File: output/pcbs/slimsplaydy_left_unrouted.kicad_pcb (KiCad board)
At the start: 2 copper layers, 115.1 x 87.3 mm, 20 parts

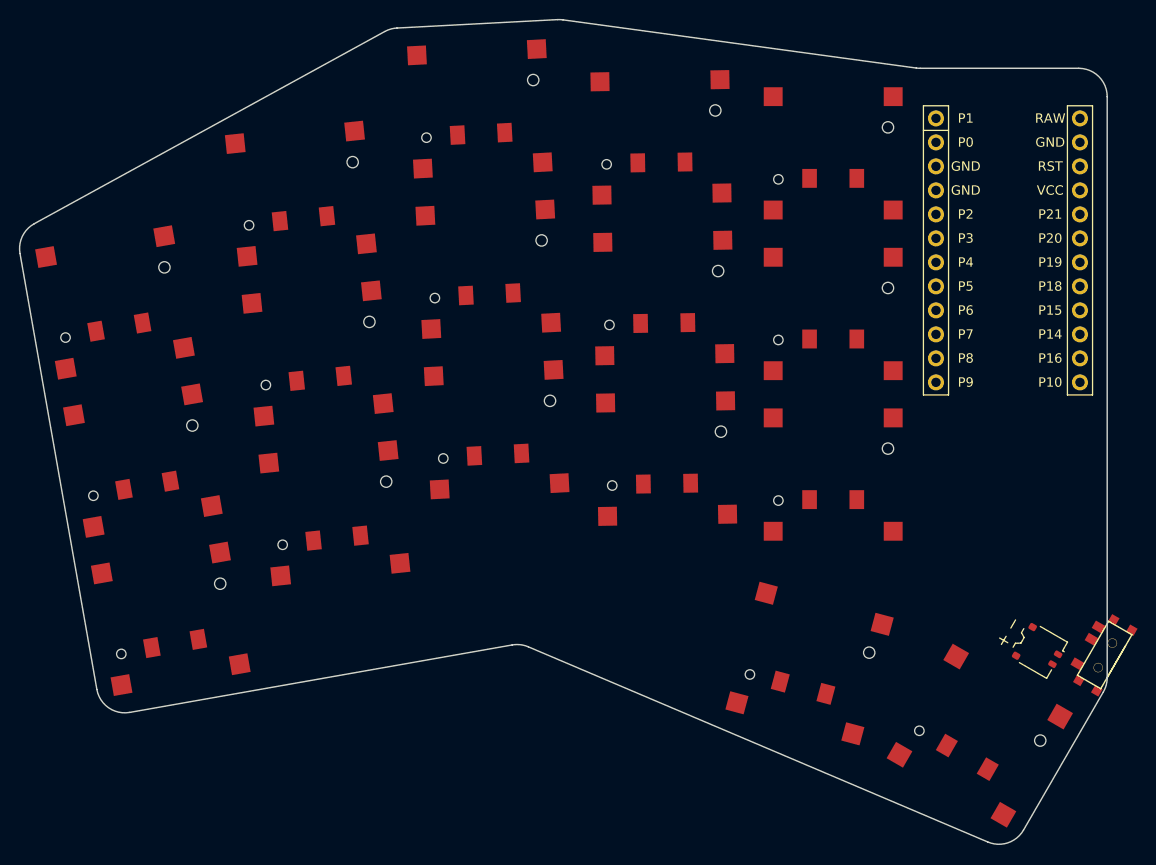
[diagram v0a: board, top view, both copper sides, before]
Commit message: Add battery footprint, change outline.
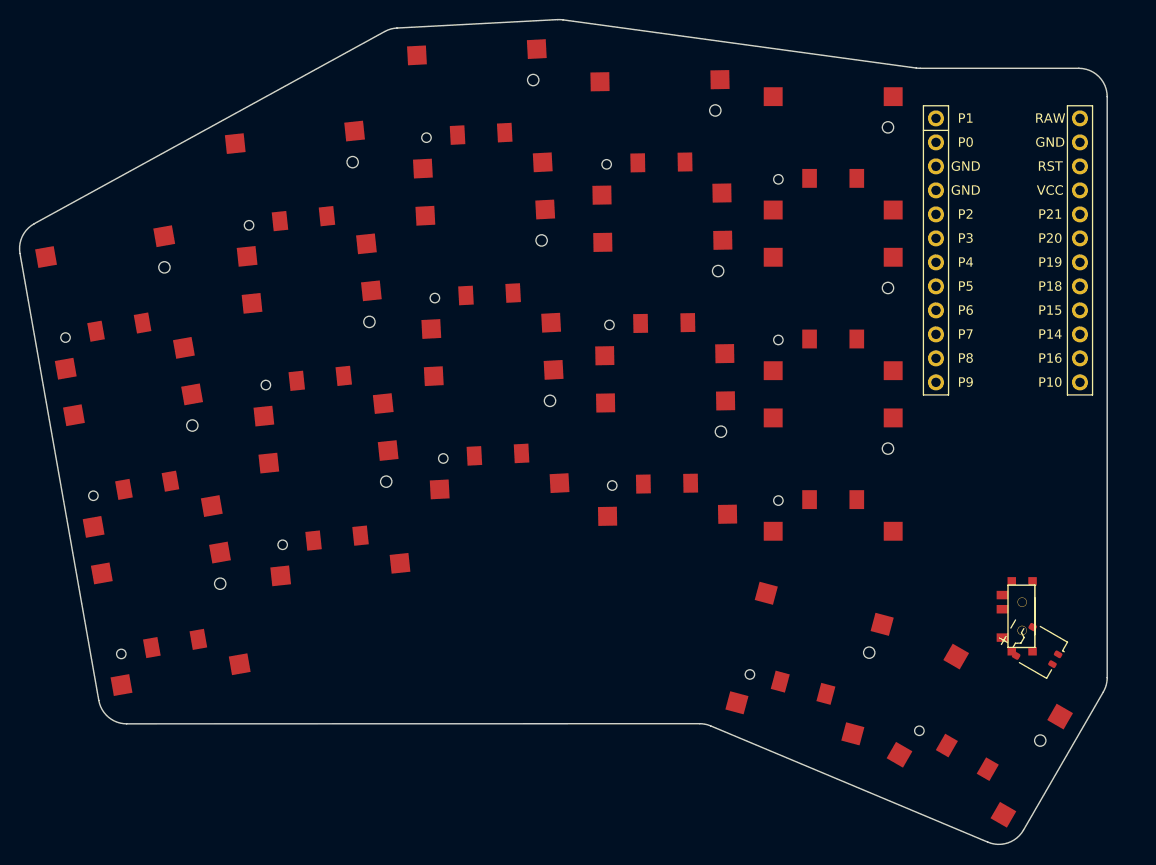
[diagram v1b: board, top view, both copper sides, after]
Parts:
- added XX1: , Battery_301230, F.Cu at (129.7, 140.4)
- moved T1 9.72 mm to (196.7, 143.4), turned to -90 degrees
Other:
- outline, holes or cut-outs redrawn
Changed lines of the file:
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@@
   )
         (module E73:SPDT_C128955 (layer F.Cu)
-            (at 205.4748588 147.5445331 -120)
+            (at 196.6773593 143.4119143 -90)
             (fp_text reference "T1" (at 0 0) (layer F.SilkS) hide (effects (font (size 1.27 1.27) (thickness 0.15))))
             (fp_text value "" (at 0 0) (layer F.SilkS) hide (effects (font (size 1.27 1.27) (thickness 0.15))))
@@
             (pad "" np_thru_hole circle (at 1.5 0) (size 1 1) (drill 0.9) (layers *.Cu *.Mask))
             (pad "" np_thru_hole circle (at -1.5 0) (size 1 1) (drill 0.9) (layers *.Cu *.Mask))
-            (pad 1 smd rect (at 2.25 2.075 -120) (size 0.9 1.25) (layers F.Cu F.Paste F.Mask) (net 67 "BAT_P"))
-            (pad 2 smd rect (at -0.75 2.075 -120) (size 0.9 1.25) (layers F.Cu F.Paste F.Mask) (net 68 "BAT"))
-            (pad 3 smd rect (at -2.25 2.075 -120) (size 0.9 1.25) (layers F.Cu F.Paste F.Mask))
-            (pad "" smd rect (at 3.7 -1.1 -120) (size 0.9 0.9) (layers F.Cu F.Paste F.Mask))
-            (pad "" smd rect (at 3.7 1.1 -120) (size 0.9 0.9) (layers F.Cu F.Paste F.Mask))
-            (pad "" smd rect (at -3.7 1.1 -120) (size 0.9 0.9) (layers F.Cu F.Paste F.Mask))
-            (pad "" smd rect (at -3.7 -1.1 -120) (size 0.9 0.9) (layers F.Cu F.Paste F.Mask))
+            (pad 1 smd rect (at 2.25 2.075 -90) (size 0.9 1.25) (layers F.Cu F.Paste F.Mask) (net 67 "BAT_P"))
+            (pad 2 smd rect (at -0.75 2.075 -90) (size 0.9 1.25) (layers F.Cu F.Paste F.Mask) (net 68 "BAT"))
+            (pad 3 smd rect (at -2.25 2.075 -90) (size 0.9 1.25) (layers F.Cu F.Paste F.Mask))
+            (pad "" smd rect (at 3.7 -1.1 -90) (size 0.9 0.9) (layers F.Cu F.Paste F.Mask))
+            (pad "" smd rect (at 3.7 1.1 -90) (size 0.9 0.9) (layers F.Cu F.Paste F.Mask))
+            (pad "" smd rect (at -3.7 1.1 -90) (size 0.9 0.9) (layers F.Cu F.Paste F.Mask))
+            (pad "" smd rect (at -3.7 -1.1 -90) (size 0.9 0.9) (layers F.Cu F.Paste F.Mask))
         )
   (footprint "ceoloide:battery_connector_molex_pico_ezmate_1x02"
@@
     (fp_line (start 0.45 2.02) (end 0.75 2.52) (layer "F.Fab") (stroke (width 0.1) (type solid)))
   )
-  (gr_line (start 205.27476762503858 151.4085073312824) (end 196.81826658790172 166.04055279537687) (angle 90) (layer Edge.Cuts) (width 0.15))
-(gr_line (start 193.047946514134 167.30060611800113) (end 144.40253976719455 146.6369199984339) (angle 90) (layer Edge.Cuts) (width 0.15))
-(gr_line (start 142.7086834385818 146.44370619182033) (end 102.22231583096315 153.58254515415393) (angle 90) (layer Edge.Cuts) (width 0.15))
-(gr_line (start 98.74694796516516 151.14906644812334) (end 90.61156255294658 105.01100333847262) (angle 90) (layer Edge.Cuts) (width 0.15))
-(gr_line (start 92.12349826198067 101.85961590074879) (end 129.22108122867328 81.51597017246681) (angle 90) (layer Edge.Cuts) (width 0.15))
+(footprint "Battery_301230"
+(at 129.6773593 140.4119143 0)
+(layer "F.Cu")
+(property "Reference" "XX1" hide (at 0 0 0) (layer "F.SilkS") (effects (font (size 1 1) (thickness 0.15))))
+(descr "Nothing but silk, 35x15 for a little extra padding")
+(tags "Battery Lithium 301230")
+(attr smd board_only exclude_from_bom)
+(embedded_fonts no)
+(zone (net 0) (net_name "") (layer "F.SilkS")  (hatch edge 0.5) (connect_pads (clearance 0)) (min_thickness 0.25) (filled_areas_thickness no) (keepout (tracks allowed) (vias allowed) (pads not_allowed) (copperpour allowed) (footprints not_allowed)) (placement (enabled no) (sheetname "")) (fill (thermal_gap 0.5) (thermal_bridge_width 0.5)) (polygon (pts (xy 129.677 140.412) (xy 163.677 140.412) (xy 163.677 154.412) (xy 129.677 154.412))))
+)
+  (gr_line (start 205.27476762503855 151.4085073312824) (end 196.812189609797 166.0510676193593) (angle 90) (layer Edge.Cuts) (width 0.15))
+(gr_line (start 193.05444906405054 167.31643081205561) (end 163.71171454116796 155.0095167067306) (angle 90) (layer Edge.Cuts) (width 0.15))
+(gr_line (start 162.55058342048673 154.77603615610332) (end 101.90742581681184 154.79218459658966) (angle 90) (layer Edge.Cuts) (width 0.15))
+(gr_line (start 98.95220363092409 152.3131292764732) (end 90.61156255219102 105.01100333888701) (angle 90) (layer Edge.Cuts) (width 0.15))
+(gr_line (start 92.12349826122507 101.85961590116315) (end 129.22108122867328 81.51597017246681) (angle 90) (layer Edge.Cuts) (width 0.15))
 (gr_line (start 130.50656080060108 81.15052443580738) (end 147.51504570837903 80.25914752326048) (angle 90) (layer Edge.Cuts) (width 0.15))
 (gr_line (start 148.07755649811176 80.28256782932584) (end 185.4755427700766 85.38438268843433) (angle 90) (layer Edge.Cuts) (width 0.15))
 (gr_line (start 185.88104555485685 85.4119144) (end 202.6773593 85.4119144) (angle 90) (layer Edge.Cuts) (width 0.15))
-(gr_line (start 205.6773593 88.4119144) (end 205.6773593 149.90735117460594) (angle 90) (layer Edge.Cuts) (width 0.15))
-(gr_arc (start 194.22085826286315 164.5393966387004) (end 193.04794646286314 167.3006061387004) (angle -82.9894051945816) (layer Edge.Cuts) (width 0.15))
-(gr_arc (start 143.22962801846543 149.39812947773467) (end 144.40253981846544 146.63691997773466) (angle -33.0149065103478) (layer Edge.Cuts) (width 0.15))
-(gr_arc (start 101.70137125107951 150.62812186823956) (end 98.7469479510795 151.14906646823957) (angle -89.99999999999747) (layer Edge.Cuts) (width 0.15))
-(gr_arc (start 93.56598583886094 104.49005875858893) (end 92.12349823886093 101.85961585858892) (angle -71.26042897748029) (layer Edge.Cuts) (width 0.15))
+(gr_line (start 205.6773593 88.4119144) (end 205.6773593 149.90735117460588) (angle 90) (layer Edge.Cuts) (width 0.15))
+(gr_arc (start 194.2147812847584 164.54991146268281) (end 193.0544490847584 167.3164307626828) (angle -82.72862751199224) (layer Edge.Cuts) (width 0.15))
+(gr_arc (start 162.55138232046008 157.77603605610335) (end 163.71171452046008 155.00951675610335) (angle -22.76938590082807) (layer Edge.Cuts) (width 0.15))
+(gr_arc (start 101.90662691683843 151.79218469658963) (end 98.95220361683843 152.31312929658964) (angle -80.01525707307042) (layer Edge.Cuts) (width 0.15))
+(gr_arc (start 93.56598583810536 104.49005875900332) (end 92.12349823810536 101.85961585900331) (angle -71.26042897748013) (layer Edge.Cuts) (width 0.15))
 (gr_arc (start 130.66356880555355 84.14641303030704) (end 130.50656080555356 81.15052443030704) (angle -25.739569207300832) (layer Edge.Cuts) (width 0.15))
 (gr_arc (start 147.6720537133315 83.25503611776017) (end 148.0775565133315 80.28256791776018) (angle -10.76831370557288) (layer Edge.Cuts) (width 0.15))
 (gr_arc (start 185.88104555485685 82.4119144) (end 185.47554275485686 85.3843826) (angle -7.768311097698927) (layer Edge.Cuts) (width 0.15))
 (gr_arc (start 202.6773593 88.4119144) (end 205.6773593 88.4119144) (angle -90) (layer Edge.Cuts) (width 0.15))
-(gr_arc (start 202.6773593 149.90735117460594) (end 205.2747677 151.40850737460593) (angle -30.02550052311193) (layer Edge.Cuts) (width 0.15))
+(gr_arc (start 202.6773593 149.90735117460588) (end 205.2747677 151.40850737460588) (angle -30.02550052311318) (layer Edge.Cuts) (width 0.15))
 )

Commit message: Complete left-side, at least to first-draft levels.
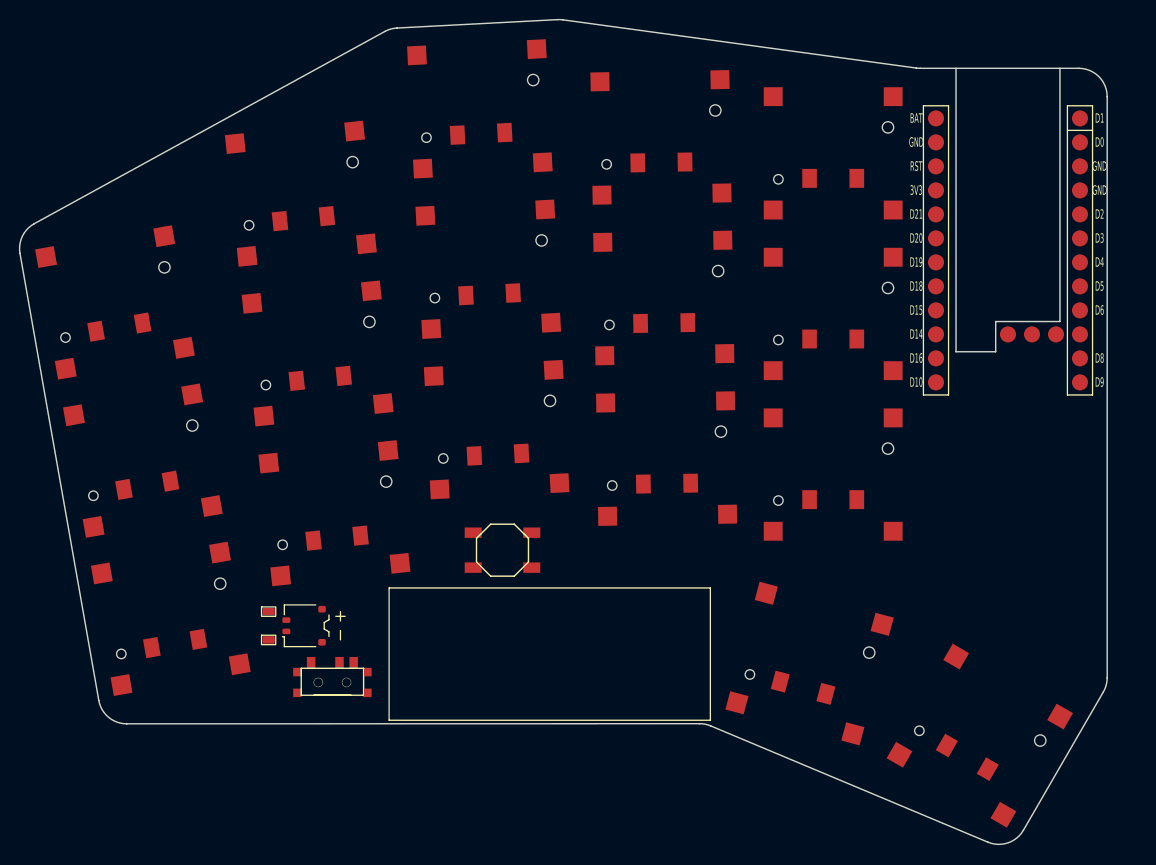
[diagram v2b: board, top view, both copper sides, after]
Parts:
- added B1: , E73:SW_TACT_ALPS_SKQGABE010, F.Cu at (141.7, 136.4)
- added XX2: , Pad_Single_BAT-, F.Cu at (116.2, 145.4)
- added XX3: , Battery_301230, F.Cu at (129.7, 140.4)
- XX1: footprint Battery_301230 -> Pad_Single_BAT-
- moved CONN1 77.9 mm to (120.7, 144.4), turned to 90 degrees
- moved T1 73.3 mm to (123.7, 150.4), turned to 180 degrees
- moved XX1 13.6 mm to (116.2, 142.4)
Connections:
- net P20 renamed D3
- net P21 renamed D2
- net RAW renamed D1
- MCU1 pad 10: P14 -> hand_ring_bottom
- MCU1 pad 11: P16 -> hand_middle_bottom
- MCU1 pad 12: P10 -> hand_index_bottom
- MCU1 pad 13: P9 -> hand_middle_home
- MCU1 pad 14: P8 -> hand_index_home
- MCU1 pad 15: P7 -> hand_inner_home
- MCU1 pad 16: P6 -> hand_pinky_top
- MCU1 pad 17: P5 -> hand_ring_top
- MCU1 pad 18: P4 -> hand_middle_top
- MCU1 pad 19: P3 -> hand_index_top
- MCU1 pad 2: GND -> D0
- MCU1 pad 20: P2 -> hand_inner_top
- MCU1 pad 21: GND -> 3V3
- MCU1 pad 22: GND -> RST
- MCU1 pad 23: P0 -> GND
- MCU1 pad 24: P1 -> BAT
- MCU1 pad 3: RST -> GND
- MCU1 pad 4: VCC -> GND
- MCU1 pad 7: P19 -> thumb_far_fan
- MCU1 pad 8: P18 -> thumb_near_fan
- MCU1 pad 9: P15 -> hand_pinky_bottom
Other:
- outline, holes or cut-outs redrawn

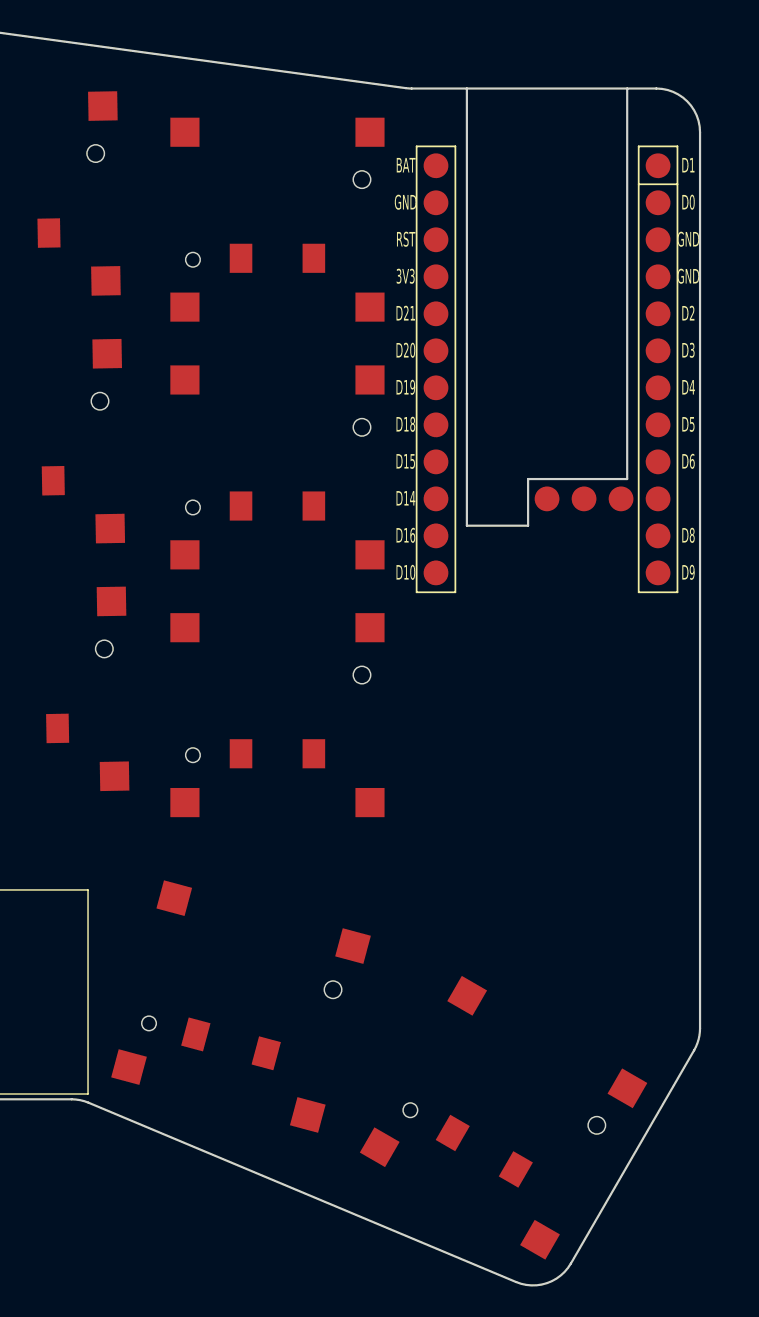
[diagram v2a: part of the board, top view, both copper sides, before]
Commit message: Create first draft design and routing for both sides.
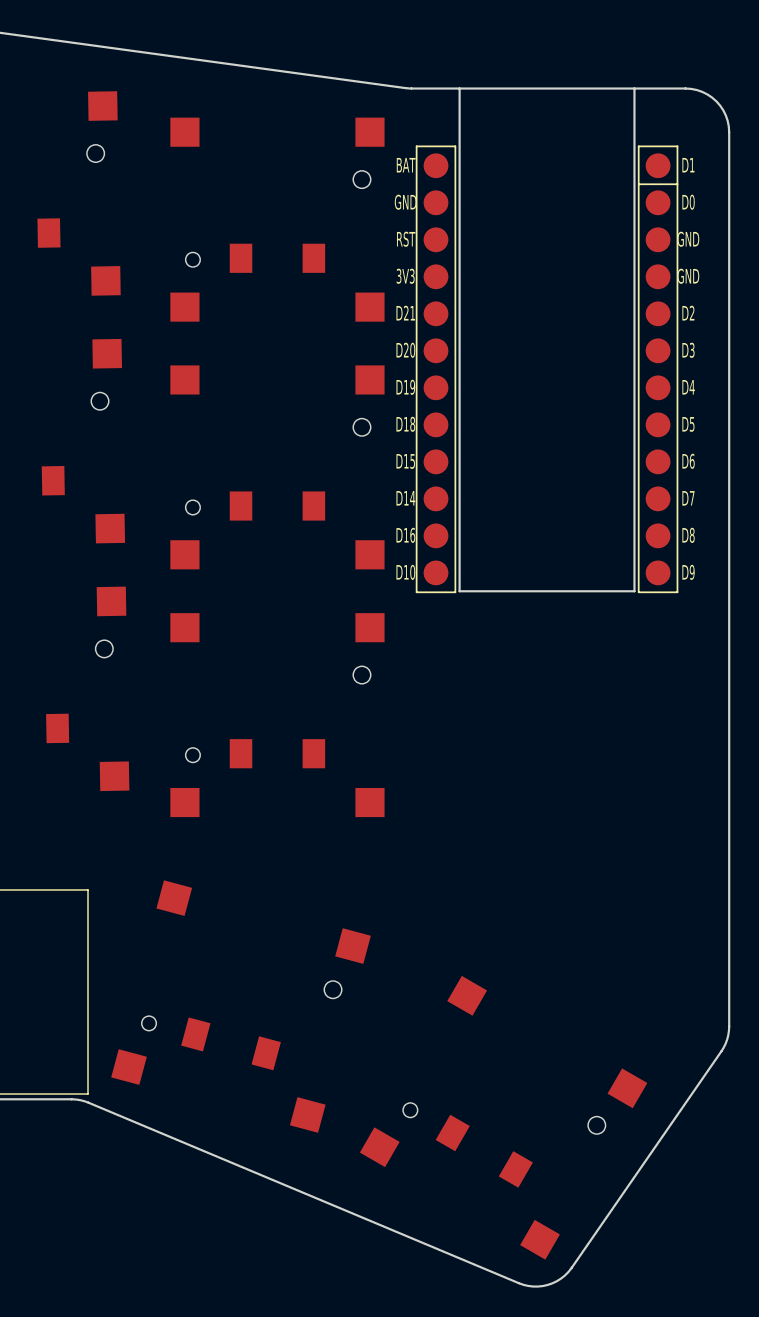
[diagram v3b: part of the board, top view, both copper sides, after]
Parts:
- XX1, XX2: footprint Pad_Single_BAT- -> Pad_Single
- moved XX3 18.4 mm to (146.7, 147.4)
- moved XX1 0.90 mm to (116.9, 142.9)
- moved XX2 0.90 mm to (116.9, 145.9)
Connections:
- MCU1 pad 10: hand_ring_bottom -> hand_pinky_home
- MCU1 pad 12: hand_index_bottom -> hand_pinky_top
- MCU1 pad 13: hand_middle_home -> hand_ring_home
- MCU1 pad 14: hand_index_home -> hand_ring_top
- MCU1 pad 16: hand_pinky_top -> hand_index_home
- MCU1 pad 17: hand_ring_top -> hand_middle_home
- MCU1 pad 2: D0 -> thumb_far_fan
- MCU1 pad 5: D2 -> thumb_near_fan
- MCU1 pad 6: D3 -> hand_pinky_bottom
- MCU1 pad 7: thumb_far_fan -> hand_ring_bottom
- MCU1 pad 8: thumb_near_fan -> hand_inner_bottom
- MCU1 pad 9: hand_pinky_bottom -> hand_index_bottom
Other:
- board size 115.1 x 87.3 mm -> 117.1 x 87.4 mm
